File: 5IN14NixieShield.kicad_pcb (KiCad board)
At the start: 2 copper layers, 110.2 x 53.6 mm, 55 parts, among them J1 I2C, J3 13, J4 EXT2, J5 UNO3, J6 UNO4, J7 UNO1, J8 UNO2, J9 EXT1, Q1 IRFD220, SW1 SW_Push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

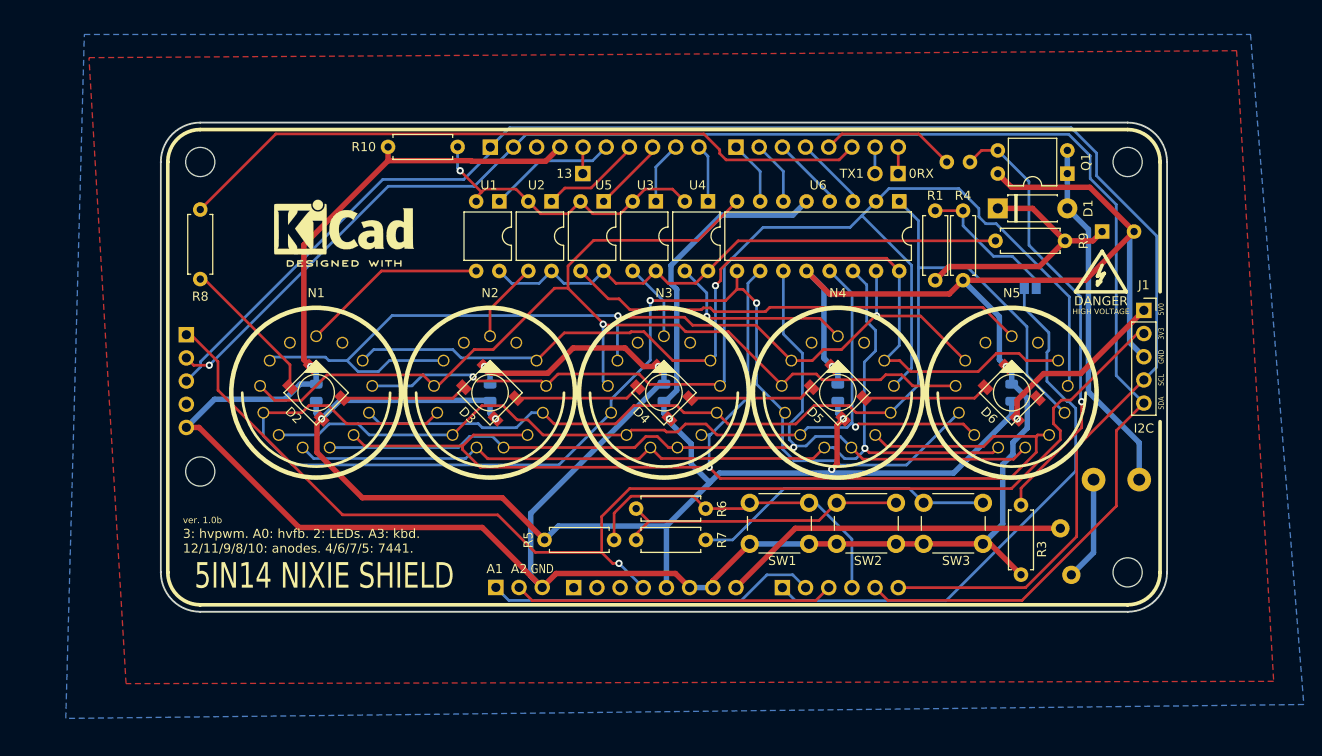
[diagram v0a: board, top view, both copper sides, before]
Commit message: Slightly optimized components placement. Added jumpers to enable decimal points (for thermometers). Updated some footprints.
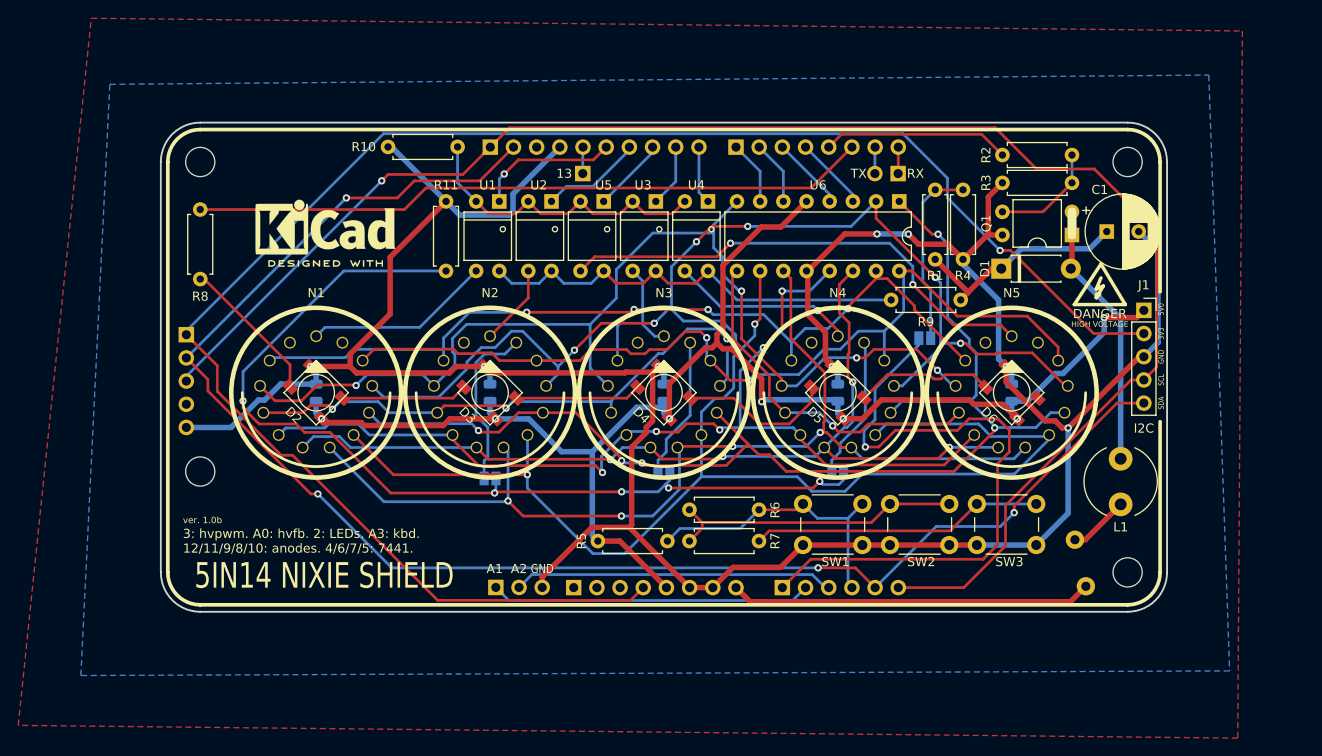
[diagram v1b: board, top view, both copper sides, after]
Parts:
- added JP2: DOT2, Jumper:SolderJumper-2_P1.3mm_Open_Pad1.0x1.5mm, B.Cu at (191.8, 151.0)
- added JP3: DOT3, Jumper:SolderJumper-2_P1.3mm_Open_Pad1.0x1.5mm, B.Cu at (210.8, 150.4)
- added JP4: DOT4, Jumper:SolderJumper-2_P1.3mm_Open_Pad1.0x1.5mm, B.Cu at (229.9, 150.4)
- added OSHW1: OSHW-Logo2_9.8x8mm_SilkScreen, Symbol:OSHW-Logo2_9.8x8mm_SilkScreen, B.Cu at (163.2, 159.3)
- added R11: 10k*, Resistor_THT:R_Axial_DIN0207_L6.3mm_D2.5mm_P7.62mm_Horizontal, F.Cu at (186.9, 120.7)
- C1, L1: moved to F.Cu
- R2: footprint Resistor_THT:R_Axial_DIN0207_L6.3mm_D2.5mm_P2.54mm_Vertical -> Resistor_THT:R_Axial_DIN0207_L6.3mm_D2.5mm_P7.62mm_Horizontal; moved to F.Cu
- U1, U2, U3, U4, U5: footprint Package_DIP:DIP-4_W7.62mm -> 5IN14Lib:TLP627
- moved R3 35.7 mm to (255.5, 118.6), turned to 180 degrees
- moved R9 13.1 mm to (243.3, 131.4)
- moved JP1 12.8 mm to (239.4, 135.6)
- moved R2 11.2 mm to (255.5, 115.6)
- moved F1 6.94 mm to (257.0, 162.8), turned to 90 degrees
- moved Q1 6.75 mm to (255.5, 124.3)
- moved D1 6.61 mm to (247.8, 128.0)
- moved SW1 5.84 mm to (226.1, 153.8)
- moved SW2 5.84 mm to (235.6, 153.8)
- moved SW3 5.84 mm to (245.1, 153.8)
- moved R6 5.84 mm to (221.2, 154.4)
- moved R7 5.84 mm to (213.6, 157.9)
- moved R5 5.84 mm to (203.6, 157.9)
- moved L1 3.06 mm to (260.9, 148.8), turned to 270 degrees
- moved R1 2.29 mm to (240.5, 119.4)
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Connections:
- D6 pad 2: (no net) -> Net-(D6-Pad2)
- J5 pad 3: (no net) -> /AREF
- J7 pad 1: (no net) -> Net-(J7-Pad1)
- J7 pad 2: (no net) -> Net-(J7-Pad2)
- J7 pad 3: (no net) -> Net-(J7-Pad3)
- N1 pad LHDP: (no net) -> Net-(N1-PadLHDP)
- N1 pad RHDP: (no net) -> Net-(N1-PadRHDP)
- N2 pad LHDP: (no net) -> Net-(N2-PadLHDP)
- N2 pad RHDP: (no net) -> Net-(JP2-Pad1)
- N3 pad LHDP: (no net) -> Net-(N3-PadLHDP)
- N3 pad RHDP: (no net) -> Net-(JP3-Pad1)
- N4 pad LHDP: (no net) -> Net-(N4-PadLHDP)
- N4 pad RHDP: (no net) -> Net-(JP4-Pad1)
- N5 pad LHDP: (no net) -> Net-(N5-PadLHDP)
- N5 pad RHDP: (no net) -> Net-(N5-PadRHDP)
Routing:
- net Net-(JP2-Pad2): track 0.00 -> 105.6 mm, vias 0 -> 5
- net +3V3: track 138.1 -> 188.9 mm
- net GND: track 344.3 -> 303.8 mm, vias 5 -> 8
- net Net-(Q1-Pad1): track 49.0 -> 12.0 mm, vias 1 -> 0
- net /NixieCtl/CATHODE_3: track 133.7 -> 97.4 mm, vias 2 -> 4
- net +5V: track 195.7 -> 161.8 mm, vias 6 -> 7
- net Net-(JP2-Pad1): track 0.00 -> 18.7 mm
- net /NixieCtl/CATHODE_8: track 112.8 -> 129.7 mm, vias 0 -> 5
- net Net-(JP4-Pad1): track 0.00 -> 15.8 mm
- net Net-(JP3-Pad1): track 0.00 -> 15.7 mm
- net /A4: track 184.2 -> 170.3 mm, vias 1 -> 4
- net /NixieCtl/CATHODE_6: track 101.2 -> 113.6 mm, vias 1 -> 4
- net Net-(R9-Pad2): track 60.2 -> 48.7 mm
- net Net-(D1-Pad2): track 39.3 -> 29.4 mm
- net /NixieCtl/CATHODE_4: track 100.1 -> 109.4 mm, vias 1 -> 5
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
